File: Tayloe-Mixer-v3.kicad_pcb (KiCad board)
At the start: 2 copper layers, 60 parts, among them J1 BNC, J101 Audio_Jack, J2 Pad, J3 Jack-DC, Q1 2N3904-SMD, Q2 2N3904-SMD, SW1 SW_DIP_x01, SW2 Rotary_Encoder_Switch, T1 6:31, T2 31:6, T3 T50_SPLITTER, U1 ESP32-A1S, U2 FST3253, U201 MAR6, U3 LM4562, U4 si5351, U5 L7805, U7 AMS1117CD-3.3

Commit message: continue
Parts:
- added J4: Conn_01x07_Female, Connector_PinSocket_2.54mm:PinSocket_1x07_P2.54mm_Vertical, F.Cu at (238.0, 82.0)
- U7: footprint Package_TO_SOT_SMD:TO-252-3_TabPin2 -> Package_TO_SOT_SMD:SOT-223-3_TabPin2
- moved SW2 260.5 mm to (347.0, 21.0), turned to 90 degrees
- moved C2 191.5 mm to (86.2, 43.4), turned to 90 degrees
- moved C4 190.7 mm to (90.1, 34.2)
- moved C3 190.1 mm to (90.1, 36.8)
- moved T1 187.4 mm to (75.8, 33.5)
- moved VC1 185.3 mm to (84.0, 33.5)
- moved C5 182.0 mm to (89.2, 43.4), turned to 90 degrees
- moved J1 179.5 mm to (58.5, 41.0), turned to 90 degrees
- moved VC6 178.3 mm to (96.0, 33.5)
- moved D1 172.9 mm to (296.0, -11.5)
- moved C201 171.7 mm to (108.0, 36.9), turned to 90 degrees
- moved T2 165.1 mm to (103.0, 33.5)
- moved C202 161.6 mm to (122.8, 36.9), turned to 270 degrees
- moved T3 146.9 mm to (124.9, 31.6)
- moved U201 115.9 mm to (115.5, 36.5), turned to 270 degrees
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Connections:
- net IO renamed IO0

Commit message: board
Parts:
- removed J2: Pad, Xenir:Pad
- moved R7 186.7 mm to (83.0, 60.6), turned to 90 degrees
- moved C14 175.3 mm to (88.0, 65.1), turned to 270 degrees
- moved C15 173.8 mm to (92.0, 64.5)
- moved C12 170.6 mm to (107.1, 52.5)
- moved U3 170.4 mm to (92.5, 57.7)
- moved C9 169.3 mm to (107.1, 60.5)
- moved C10 168.9 mm to (107.0, 56.5)
- moved R6 166.7 mm to (112.1, 52.5)
- moved R3 164.7 mm to (112.1, 60.5)
- moved R4 164.3 mm to (112.1, 56.5)
- moved C11 162.7 mm to (107.0, 64.5)
- moved R5 155.6 mm to (112.0, 64.5)
- moved R8 150.5 mm to (96.0, 58.4), turned to 90 degrees
- moved C13 149.8 mm to (92.5, 53.5)
- moved U2 143.6 mm to (119.5, 61.2), turned to 90 degrees
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
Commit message: gg
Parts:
- moved J3 46.4 mm to (204.0, 91.0)
- moved U7 24.2 mm to (179.5, 95.7), turned to 90 degrees
- moved C25 21.5 mm to (188.9, 105.2)
- moved C6 21.5 mm to (182.5, 105.7)
- moved C7 21.5 mm to (187.5, 86.2)
- moved R1 21.5 mm to (179.0, 103.0)
- moved R2 21.5 mm to (179.0, 107.6)
- moved U5 21.5 mm to (192.0, 96.5)
- moved U1 18.7 mm to (98.9, 107.3), turned to 180 degrees
- moved C103 9.12 mm to (89.6, 68.2)
- moved C8 6.22 mm to (119.4, 70.2)
- moved R5 6.18 mm to (110.5, 70.5), turned to 180 degrees
- moved U2 6.05 mm to (113.5, 61.0)
- moved R8 5.50 mm to (96.0, 63.9)
- moved R7 5.10 mm to (88.0, 61.1), turned to 270 degrees
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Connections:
- R5 pad 2: Net-(C15-Pad2) -> Net-(R5-Pad2)
- R6 pad 2: Net-(R6-Pad2) -> Net-(C15-Pad2)
- U3 pad 5: Net-(R6-Pad2) -> Net-(R5-Pad2)
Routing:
- net +12V: track 0.00 -> 47.7 mm
- net Net-(C15-Pad2): track 0.00 -> 34.4 mm, vias 0 -> 2
- net Net-(C14-Pad2): track 0.00 -> 34.0 mm, vias 0 -> 2
- net Net-(R4-Pad2): track 0.00 -> 31.2 mm
- net I_SIGNAL: track 0.00 -> 28.2 mm
- net Net-(C6-Pad1): track 0.00 -> 24.3 mm
- net Q_SIGNAL: track 0.00 -> 20.4 mm, vias 0 -> 2
- net Net-(C3-Pad2): track 0.00 -> 19.4 mm
- net +5V: track 0.00 -> 18.2 mm
- net Net-(J1-PadS): track 0.00 -> 18.0 mm
- net Net-(R5-Pad2): track 0.00 -> 16.1 mm
- net Net-(C2-Pad2): track 0.00 -> 15.4 mm
- net RTS: track 0.00 -> 15.4 mm
- net EN: track 0.00 -> 13.7 mm
- net Net-(C11-Pad2): track 0.00 -> 12.1 mm
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
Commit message: updating pcb
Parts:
- moved SW2 305.4 mm to (51.0, 96.0)
- moved D1 210.8 mm to (96.5, 56.5)
- moved J3 65.8 mm to (141.0, 72.0)
- moved C7 55.9 mm to (132.8, 74.5), turned to 180 degrees
- moved C25 48.4 mm to (141.9, 93.8)
- moved C6 48.4 mm to (135.5, 94.2)
- moved R1 48.4 mm to (132.0, 91.5)
- moved R2 48.4 mm to (132.0, 96.1)
- moved U5 48.4 mm to (145.0, 85.0)
- moved U7 48.4 mm to (132.5, 84.2)
- moved U1 35.4 mm to (68.9, 88.5), turned to 90 degrees
- moved J4 25.2 mm to (120.0, 97.5)
- moved Q1 25.2 mm to (114.0, 88.0)
- moved Q2 25.2 mm to (120.0, 88.0)
- moved R10 25.2 mm to (120.1, 80.9)
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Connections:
- U1 pad 1: Net-(U1-Pad1) -> GND
- U1 pad 2: Net-(U1-Pad2) -> +3V3
- U1 pad 21: Net-(C103-Pad2) -> Net-(C104-Pad2)
- U1 pad 22: Net-(C104-Pad2) -> Net-(C103-Pad2)
- U4 pad SCL: Net-(U4-PadSCL) -> SCL
- U4 pad SDA: Net-(U4-PadSDA) -> SDA
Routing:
- net +12V: track 47.7 -> 154.2 mm, vias 0 -> 3
- net TX0: track 0.00 -> 57.1 mm, vias 0 -> 1
- net RX0: track 0.00 -> 54.0 mm, vias 0 -> 1
- net Net-(SW2-PadS2): track 0.00 -> 44.8 mm, vias 0 -> 1
- net Net-(SW2-PadA): track 0.00 -> 42.7 mm, vias 0 -> 1
- net +3V3: track 6.30 -> 39.1 mm, vias 0 -> 1
- net Net-(SW2-PadB): track 0.00 -> 32.1 mm, vias 0 -> 1
- net EN: track 13.7 -> 44.7 mm
- net OUTL: track 0.00 -> 25.4 mm
- net SDA: track 0.00 -> 24.5 mm, vias 0 -> 1
- net Net-(T3-PadC3A): track 0.00 -> 22.6 mm
- net SCL: track 0.00 -> 22.0 mm, vias 0 -> 1
- net OUTR: track 0.00 -> 15.3 mm
- net Net-(T3-PadC2B): track 0.00 -> 14.4 mm
- net RTS: track 15.4 -> 29.4 mm, vias 0 -> 1
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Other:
- board outline added: 109 x 76.5 mm

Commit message: rerouting
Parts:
- moved U4 34.2 mm to (151.2, 60.5), turned to 90 degrees
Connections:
- U1 pad 10: Net-(SW2-PadB) -> Net-(SW2-PadA)
- U1 pad 12: Net-(SW2-PadA) -> Net-(SW2-PadS2)
- U1 pad 6: Net-(U1-Pad6) -> IO0
- U1 pad 8: Net-(SW2-PadS2) -> Net-(SW2-PadB)
- U4 pad 0: Net-(U2-Pad14) -> Net-(U2-Pad2)
- U4 pad 2: Net-(U2-Pad2) -> Net-(U2-Pad14)
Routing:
- net +3V3: track 39.1 -> 155.1 mm, vias 1 -> 2
- net SDA: track 24.5 -> 130.1 mm, vias 1 -> 3
- net SCL: track 22.0 -> 126.0 mm
- net +5V: track 22.1 -> 117.5 mm, vias 0 -> 2
- net IO0: track 0.00 -> 82.6 mm, vias 0 -> 2
- net Net-(U2-Pad14): track 0.00 -> 54.6 mm, vias 0 -> 1
- net Net-(U2-Pad2): track 0.00 -> 35.6 mm, vias 0 -> 1
- net Net-(C10-Pad2): track 7.58 -> 38.6 mm, vias 0 -> 2
- net Net-(C9-Pad2): track 8.67 -> 32.3 mm, vias 0 -> 2
- net Net-(C11-Pad2): track 12.1 -> 28.7 mm, vias 0 -> 2
- net +12V: track 154.2 -> 169.2 mm
- net Net-(C12-Pad2): track 9.92 -> 19.5 mm
- net Net-(SW2-PadS2): track 44.8 -> 48.7 mm
- net Net-(SW2-PadA): track 42.7 -> 40.2 mm
- net Net-(SW2-PadB): track 32.1 -> 30.4 mm

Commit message: finished?
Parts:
- removed D1: LCD_I2C, xenir:LCD_I2C
- added J2: Conn_01x04, Connector_PinSocket_2.54mm:PinSocket_1x04_P2.54mm_Vertical, F.Cu at (63.5, 69.5)
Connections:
- net Net-(C6-Pad1) renamed 2.5V
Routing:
- net 2.5V: track 24.3 -> 121.4 mm
- net Q_SIGNAL: track 21.2 -> 24.2 mm
- net Net-(C3-Pad2): track 19.4 -> 21.9 mm
- net GND: vias 0 -> 6
- added copper zone on B.Cu, net GND
- added copper zone on F.Cu, net GND

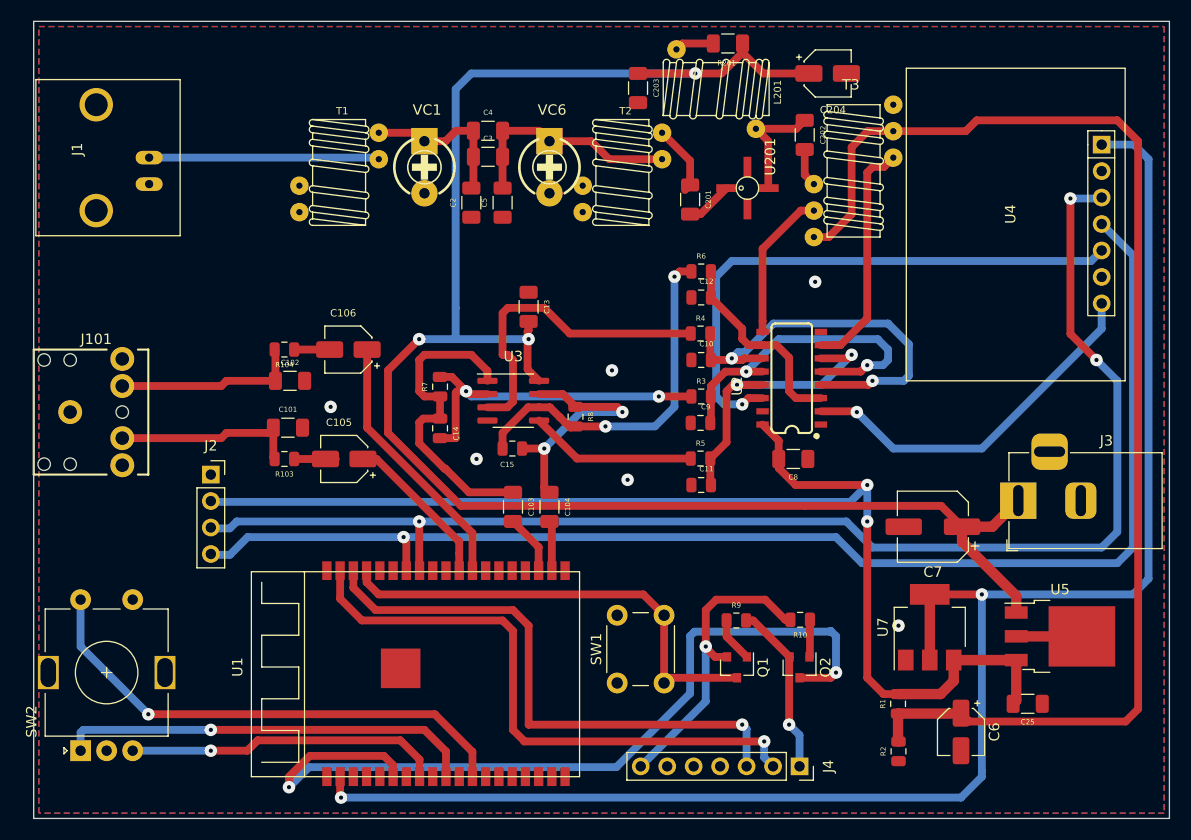
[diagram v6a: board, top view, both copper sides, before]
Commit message: fixed audio jack
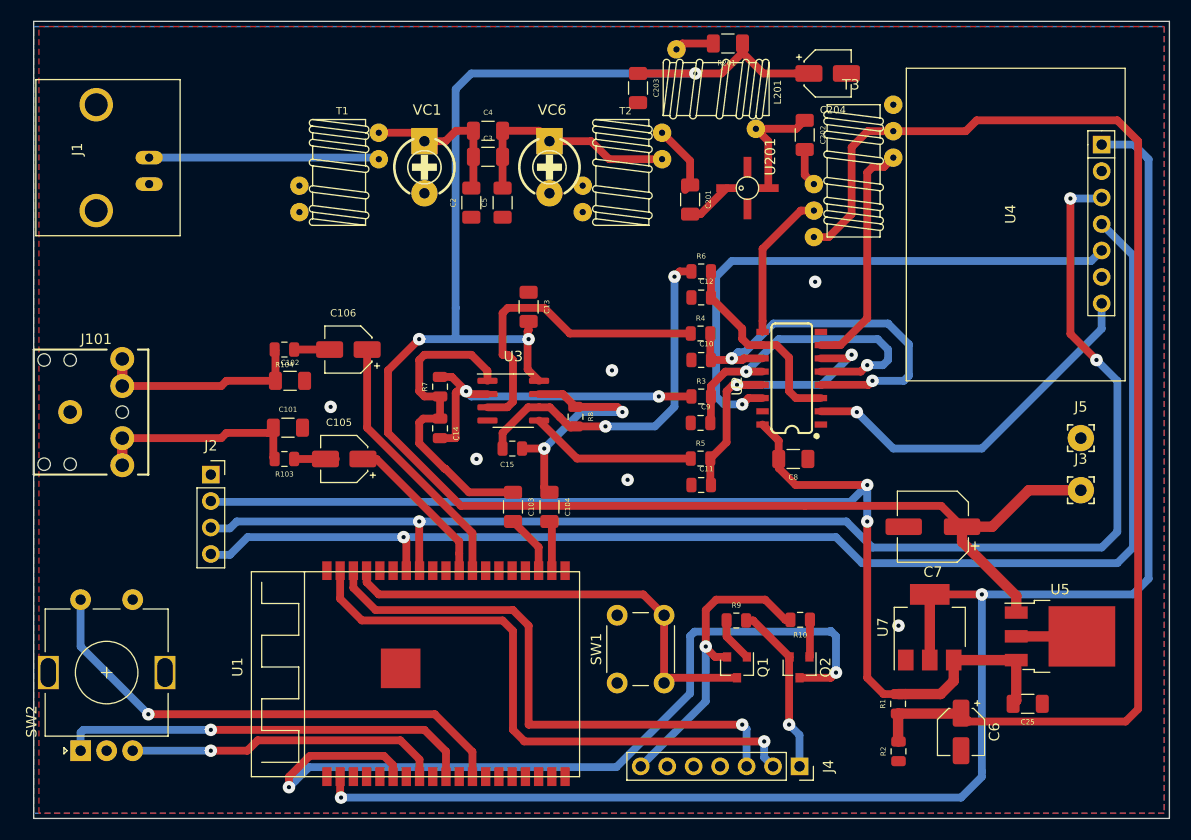
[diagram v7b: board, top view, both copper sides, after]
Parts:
- added J5: Pad, Xenir:Pad, F.Cu at (147.0, 62.5)
- J3: value Jack-DC -> Pad; footprint Connector_BarrelJack:BarrelJack_Horizontal -> Xenir:Pad
- moved J3 7.50 mm to (147.0, 67.5), turned to 0 degrees
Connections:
- J101 pad RING: Net-(J101-PadRING) -> Net-(C102-Pad1)
- J101 pad TIP: Net-(J101-PadTIP) -> Net-(C101-Pad1)
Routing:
- net +12V: track 169.2 -> 175.6 mm
- net Net-(C102-Pad1): track 17.9 -> 20.5 mm
- net Net-(C101-Pad1): track 18.0 -> 20.6 mm

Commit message: gg
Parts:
- moved J101 0.50 mm to (52.0, 54.5)
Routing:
- net Net-(C101-Pad1): track 20.6 -> 20.4 mm, vias 0 -> 1
- net Net-(C102-Pad1): track 20.5 -> 20.4 mm, vias 0 -> 1
- net GND: vias 6 -> 5
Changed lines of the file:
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@@
     (thickness 1.6)
     (drawings 4)
-    (tracks 449)
+    (tracks 451)
     (zones 0)
     (modules 61)
@@
   )
   (module xenir:Audio_Jack (layer F.Cu)
-    (at 52 55)
+    (at 52 54.5)
     (fp_text reference J101 (at 0.5 1.5) (layer F.SilkS)
       (effects (font (size 1 1) (thickness 0.15)))
@@
   (via (at 129.5 84) (size 1.2) (drill 0.4) (layers F.Cu B.Cu) (net 1))
   (via (at 89 68) (size 1.2) (drill 0.4) (layers F.Cu B.Cu) (net 1))
-  (via (at 75 63) (size 1.2) (drill 0.4) (layers F.Cu B.Cu) (net 1))
   (via (at 121.5 51) (size 1.2) (drill 0.4) (layers F.Cu B.Cu) (net 1))
   (via (at 102 59.5) (size 1.2) (drill 0.4) (layers F.Cu B.Cu) (net 1))
@@
   (via (at 103 63.5) (size 1.2) (drill 0.4) (layers F.Cu B.Cu) (net 6))
   (segment (start 99 63.5) (end 103 63.5) (width 0.75) (layer B.Cu) (net 6))
-  (segment (start 69 65.5) (end 69.5 65) (width 0.75) (layer F.Cu) (net 7))
-  (segment (start 65 65.5) (end 69 65.5) (width 0.75) (layer F.Cu) (net 7))
   (segment (start 69.5 67.875) (end 69.625 68) (width 0.75) (layer F.Cu) (net 7))
   (segment (start 69.5 65) (end 69.5 67.875) (width 0.75) (layer F.Cu) (net 7))
-  (segment (start 64.5 66) (end 55 66) (width 0.75) (layer F.Cu) (net 7))
-  (segment (start 65 65.5) (end 64.5 66) (width 0.75) (layer F.Cu) (net 7))
-  (segment (start 55 66) (end 55 68.6) (width 1) (layer F.Cu) (net 7))
-  (segment (start 65 60.5) (end 69.7 60.5) (width 0.75) (layer F.Cu) (net 8))
+  (segment (start 55 68.1) (end 55 65.5) (width 1) (layer B.Cu) (net 7))
+  (segment (start 55 65.5) (end 62.5 65.5) (width 1) (layer B.Cu) (net 7))
+  (segment (start 62.5 65.5) (end 62.5 65.5) (width 1) (layer B.Cu) (net 7))
+  (via (at 62.5 65.5) (size 1.2) (drill 0.4) (layers F.Cu B.Cu) (net 7))
+  (segment (start 69 65.5) (end 69.5 65) (width 1) (layer F.Cu) (net 7))
+  (segment (start 62.5 65.5) (end 69 65.5) (width 1) (layer F.Cu) (net 7))
   (segment (start 69.7 57.575) (end 69.625 57.5) (width 0.75) (layer F.Cu) (net 8))
   (segment (start 69.7 60.5) (end 69.7 57.575) (width 0.75) (layer F.Cu) (net 8))
-  (segment (start 64.5 61) (end 65 60.5) (width 0.75) (layer F.Cu) (net 8))
-  (segment (start 55 61) (end 64.5 61) (width 0.75) (layer F.Cu) (net 8))
-  (segment (start 55 58.4) (end 55 61) (width 1) (layer F.Cu) (net 8))
+  (segment (start 55 60.5) (end 55 57.9) (width 1) (layer B.Cu) (net 8))
+  (segment (start 55 57.9) (end 62.4 57.9) (width 1) (layer B.Cu) (net 8))
+  (segment (start 62.4 57.9) (end 62.4 57.9) (width 1) (layer B.Cu) (net 8))
+  (via (at 62.4 57.9) (size 1.2) (drill 0.4) (layers F.Cu B.Cu) (net 8))
+  (segment (start 69.225 57.9) (end 69.625 57.5) (width 1) (layer F.Cu) (net 8))
+  (segment (start 62.4 57.9) (end 69.225 57.9) (width 1) (layer F.Cu) (net 8))
   (segment (start 94.96 76.46) (end 94.96 78.717) (width 0.75) (layer F.Cu) (net 9))
   (segment (start 92.5 74) (end 94.96 76.46) (width 0.75) (layer F.Cu) (net 9))
@@
     (polygon
       (pts
-        (xy 155 102) (xy 47 102) (xy 47 26.5) (xy 155 26.5)
+        (xy 155.5 102.5) (xy 46.5 102.5) (xy 46.5 26.5) (xy 155.5 26.5)
       )
     )
@@
     (polygon
       (pts
-        (xy 155 102) (xy 46.5 102) (xy 46.5 26.5) (xy 155 26.5)
+        (xy 155 102.5) (xy 47 102.5) (xy 47 26.5) (xy 155 26.5)
       )
     )
